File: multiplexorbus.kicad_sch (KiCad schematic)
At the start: 6 parts

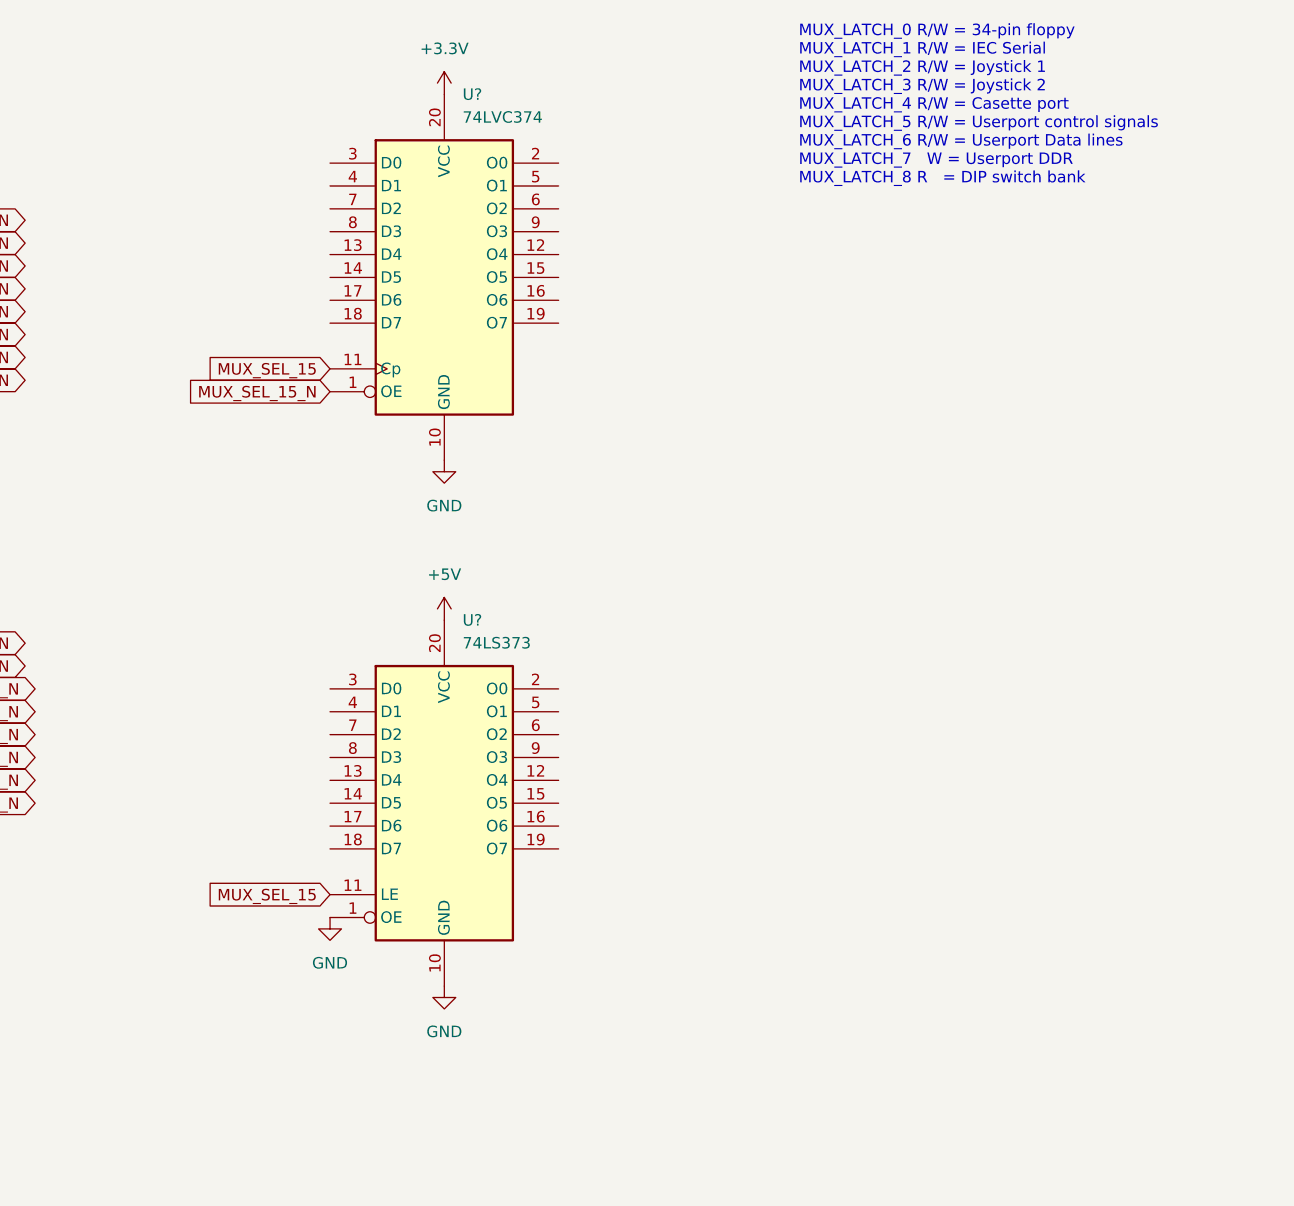
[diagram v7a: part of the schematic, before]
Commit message: hook up expansion port using MUX bus
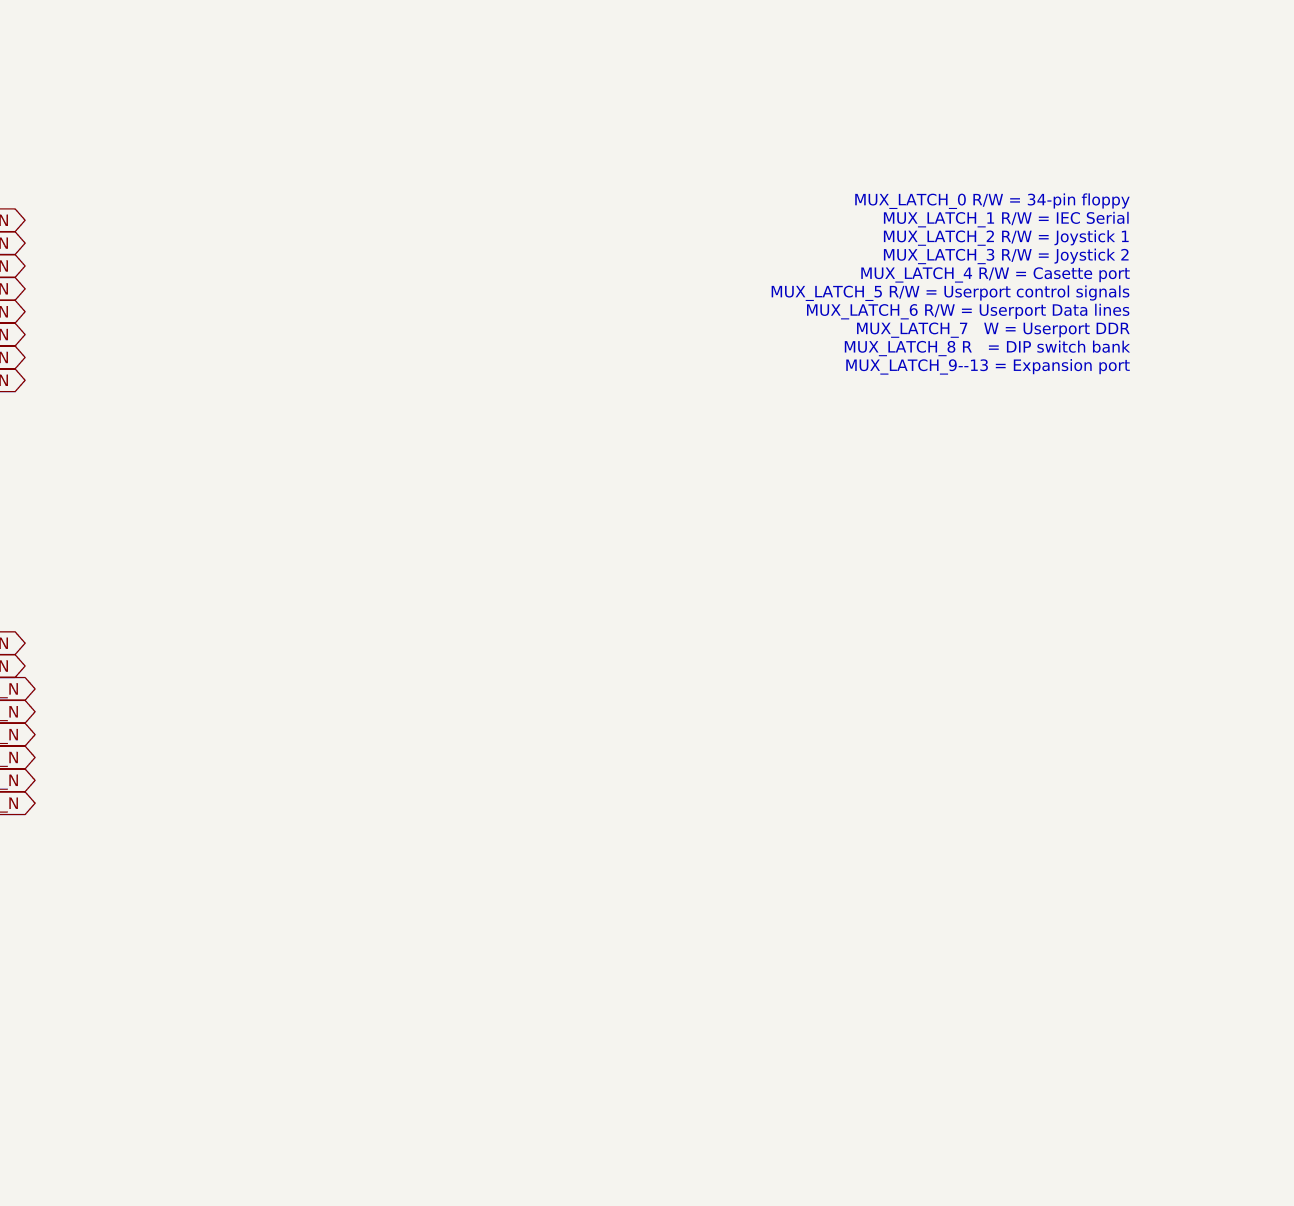
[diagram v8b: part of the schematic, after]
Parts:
- removed U?: 74LS373, Package_DIP:DIP-20_W7.62mm, symbol 74xx:74LS373
- removed U?: 74LVC374, Package_DIP:DIP-20_W7.62mm, symbol 74xx:74HC374
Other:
- note added: "MUX_LATCH_0 R/W = 34-pin floppy MUX_LATCH_1 R/W = IEC Serial MUX_LATCH_2 R/W = Joystick 1 MUX_LATCH_3 R/W = Joystick 2 MUX_LATCH_4 R/W = Casette port MUX_LATCH_5 R/W = Userport control signals MUX_LATCH_6 R/W = Userport Data lines MUX_LATCH_7 W = Userport DDR MUX_LATCH_8 R = DIP switch bank MUX_LATCH_9--13 = Expansion port"
- note removed: "MUX_LATCH_0 R/W = 34-pin floppy MUX_LATCH_1 R/W = IEC Serial MUX_LATCH_2 R/W = Joystick 1 MUX_LATCH_3 R/W = Joystick 2 MUX_LATCH_4 R/W = Casette port MUX_LATCH_5 R/W = Userport control signals MUX_LATCH_6 R/W = Userport Data lines MUX_LATCH_7 W = Userport DDR MUX_LATCH_8 R = DIP switch bank"
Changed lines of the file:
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@@
     (effects (font (size 1.27 1.27)) (justify left bottom))
   )
-  (text "MUX_LATCH_0 R/W = 34-pin floppy\nMUX_LATCH_1 R/W = IEC Serial\nMUX_LATCH_2 R/W = Joystick 1\nMUX_LATCH_3 R/W = Joystick 2\nMUX_LATCH_4 R/W = Casette port\nMUX_LATCH_5 R/W = Userport control signals\nMUX_LATCH_6 R/W = Userport Data lines\nMUX_LATCH_7   W = Userport DDR\nMUX_LATCH_8 R   = DIP switch bank"
-    (at 233.68 29.21 0)
-    (effects (font (size 1.27 1.27)) (justify left bottom))
+  (text "MUX_LATCH_0 R/W = 34-pin floppy\nMUX_LATCH_1 R/W = IEC Serial\nMUX_LATCH_2 R/W = Joystick 1\nMUX_LATCH_3 R/W = Joystick 2\nMUX_LATCH_4 R/W = Casette port\nMUX_LATCH_5 R/W = Userport control signals\nMUX_LATCH_6 R/W = Userport Data lines\nMUX_LATCH_7   W = Userport DDR\nMUX_LATCH_8 R   = DIP switch bank\nMUX_LATCH_9--13 = Expansion port"
+    (at 270.51 50.165 0)
+    (effects (font (size 1.27 1.27)) (justify right bottom))
   )
   (text "MUX_Ax are 3.3V signals" (at 38.1 29.21 180)
@@
     )
   )
-  (global_label "MUX_SEL_15" (shape input) (at 181.61 107.95 180) (fields_autoplaced)
-    (effects (font (size 1.27 1.27)) (justify right))
-    (property "Intersheet References" "${INTERSHEET_REFS}" (id 0) (at 167.4645 107.8706 0)
-      (effects (font (size 1.27 1.27)) (justify right) hide)
-    )
-  )
   (global_label "MUX_A2" (shape input) (at 107.95 85.09 180) (fields_autoplaced)
     (effects (font (size 1.27 1.27)) (justify right))
@@
     )
   )
-  (global_label "MUX_SEL_15" (shape input) (at 181.61 49.53 180) (fields_autoplaced)
-    (effects (font (size 1.27 1.27)) (justify right))
-    (property "Intersheet References" "${INTERSHEET_REFS}" (id 0) (at 167.4645 49.4506 0)
-      (effects (font (size 1.27 1.27)) (justify right) hide)
-    )
-  )
-  (global_label "MUX_SEL_15_N" (shape input) (at 181.61 52.07 180) (fields_autoplaced)
-    (effects (font (size 1.27 1.27)) (justify right))
-    (property "Intersheet References" "${INTERSHEET_REFS}" (id 0) (at 165.1664 51.9906 0)
-      (effects (font (size 1.27 1.27)) (justify right) hide)
-    )
-  )
   (global_label "MUX_SEL_11_N" (shape output) (at 133.35 87.63 0) (fields_autoplaced)
     (effects (font (size 1.27 1.27)) (justify left))
@@
       (effects (font (size 1.27 1.27)) (justify left) hide)
     )
-  )
-  (symbol (lib_id "power:+5V") (at 194.31 77.47 0) (unit 1)
-    (in_bom yes) (on_board yes) (fields_autoplaced)
-    (property "Reference" "#PWR?" (id 0) (at 194.31 81.28 0)
-      (effects (font (size 1.27 1.27)) hide)
-    )
-    (property "Value" "+5V" (id 1) (at 194.31 72.39 0))
-    (property "Footprint" "" (id 2) (at 194.31 77.47 0)
-      (effects (font (size 1.27 1.27)) hide)
-    )
-    (property "Datasheet" "" (id 3) (at 194.31 77.47 0)
-      (effects (font (size 1.27 1.27)) hide)
-    )
-    (pin "1")
   )
   (symbol (lib_id "74xx:74LS138") (at 120.65 87.63 0) (unit 1)
@@
     (pin "1")
   )
-  (symbol (lib_id "power:GND") (at 194.31 118.11 0) (unit 1)
-    (in_bom yes) (on_board yes) (fields_autoplaced)
-    (property "Reference" "#PWR?" (id 0) (at 194.31 124.46 0)
-      (effects (font (size 1.27 1.27)) hide)
-    )
-    (property "Value" "GND" (id 1) (at 194.31 123.19 0))
-    (property "Footprint" "" (id 2) (at 194.31 118.11 0)
-      (effects (font (size 1.27 1.27)) hide)
-    )
-    (property "Datasheet" "" (id 3) (at 194.31 118.11 0)
-      (effects (font (size 1.27 1.27)) hide)
-    )
-    (pin "1")
-  )
   (symbol (lib_id "power:GND") (at 120.65 105.41 0) (unit 1)
     (in_bom yes) (on_board yes) (fields_autoplaced)
@@
     (pin "1")
   )
-  (symbol (lib_id "74xx:74LS373") (at 194.31 97.79 0) (unit 1)
-    (in_bom yes) (on_board yes) (fields_autoplaced)
-    (property "Reference" "U?" (id 0) (at 196.3294 77.47 0)
-      (effects (font (size 1.27 1.27)) (justify left))
-    )
-    (property "Value" "74LS373" (id 1) (at 196.3294 80.01 0)
-      (effects (font (size 1.27 1.27)) (justify left))
-    )
-    (property "Footprint" "Package_DIP:DIP-20_W7.62mm" (id 2) (at 194.31 97.79 0)
-      (effects (font (size 1.27 1.27)) hide)
-    )
-    (property "Datasheet" "http://www.ti.com/lit/gpn/sn74LS373" (id 3) (at 194.31 97.79 0)
-      (effects (font (size 1.27 1.27)) hide)
-    )
-    (pin "1")
-    (pin "10")
-    (pin "11")
-    (pin "12")
-    (pin "13")
-    (pin "14")
-    (pin "15")
-    (pin "16")
-    (pin "17")
-    (pin "18")
-    (pin "19")
-    (pin "2")
-    (pin "20")
-    (pin "3")
-    (pin "4")
-    (pin "5")
-    (pin "6")
-    (pin "7")
-    (pin "8")
-    (pin "9")
-  )
   (symbol (lib_id "power:GND") (at 53.34 58.42 0) (unit 1)
     (in_bom yes) (on_board yes) (fields_autoplaced)
@@
     )
     (pin "1")
-  )
-  (symbol (lib_id "74xx:74HC374") (at 194.31 39.37 0) (unit 1)
-    (in_bom yes) (on_board yes) (fields_autoplaced)
-    (property "Reference" "U?" (id 0) (at 196.3294 19.05 0)
-      (effects (font (size 1.27 1.27)) (justify left))
-    )
-    (property "Value" "74LVC374" (id 1) (at 196.3294 21.59 0)
-      (effects (font (size 1.27 1.27)) (justify left))
-    )
-    (property "Footprint" "Package_DIP:DIP-20_W7.62mm" (id 2) (at 194.31 39.37 0)
-      (effects (font (size 1.27 1.27)) hide)
-    )
-    (property "Datasheet" "https://www.ti.com/lit/ds/symlink/cd74hct374.pdf" (id 3) (at 194.31 39.37 0)
-      (effects (font (size 1.27 1.27)) hide)
-    )
-    (pin "1")
-    (pin "10")
-    (pin "11")
-    (pin "12")
-    (pin "13")
-    (pin "14")
-    (pin "15")
-    (pin "16")
-    (pin "17")
-    (pin "18")
-    (pin "19")
-    (pin "2")
-    (pin "20")
-    (pin "3")
-    (pin "4")
-    (pin "5")
-    (pin "6")
-    (pin "7")
-    (pin "8")
-    (pin "9")
   )
   (symbol (lib_id "power:+3.3V") (at 120.65 73.66 0) (unit 1)
@@
     (pin "9")
   )
-  (symbol (lib_id "power:GND") (at 194.31 59.69 0) (unit 1)
-    (in_bom yes) (on_board yes) (fields_autoplaced)
-    (property "Reference" "#PWR?" (id 0) (at 194.31 66.04 0)
-      (effects (font (size 1.27 1.27)) hide)
-    )
-    (property "Value" "GND" (id 1) (at 194.31 64.77 0))
-    (property "Footprint" "" (id 2) (at 194.31 59.69 0)
-      (effects (font (size 1.27 1.27)) hide)
-    )
-    (property "Datasheet" "" (id 3) (at 194.31 59.69 0)
-      (effects (font (size 1.27 1.27)) hide)
-    )
-    (pin "1")
-  )
   (symbol (lib_id "power:+5V") (at 107.95 45.72 0) (unit 1)
     (in_bom yes) (on_board yes) (fields_autoplaced)
@@
     )
     (property "Datasheet" "" (id 3) (at 40.64 45.72 0)
-      (effects (font (size 1.27 1.27)) hide)
-    )
-    (pin "1")
-  )
-  (symbol (lib_id "power:+3.3V") (at 194.31 19.05 0) (unit 1)
-    (in_bom yes) (on_board yes) (fields_autoplaced)
-    (property "Reference" "#PWR?" (id 0) (at 194.31 22.86 0)
-      (effects (font (size 1.27 1.27)) hide)
-    )
-    (property "Value" "+3.3V" (id 1) (at 194.31 13.97 0))
-    (property "Footprint" "" (id 2) (at 194.31 19.05 0)
-      (effects (font (size 1.27 1.27)) hide)
-    )
-    (property "Datasheet" "" (id 3) (at 194.31 19.05 0)
       (effects (font (size 1.27 1.27)) hide)
     )
@@
       (effects (font (size 1.27 1.27)) hide)
     )
-    (pin "1")
-  )
-  (symbol (lib_id "power:GND") (at 181.61 110.49 0) (unit 1)
-    (in_bom yes) (on_board yes) (fields_autoplaced)
-    (property "Reference" "#PWR?" (id 0) (at 181.61 116.84 0)
-      (effects (font (size 1.27 1.27)) hide)
-    )
-    (property "Value" "GND" (id 1) (at 181.61 115.57 0))
-    (property "Footprint" "" (id 2) (at 181.61 110.49 0)
-      (effects (font (size 1.27 1.27)) hide)
-    )
-    (property "Datasheet" "" (id 3) (at 181.61 110.49 0)
-      (effects (font (size 1.27 1.27)) hide)
-    )
